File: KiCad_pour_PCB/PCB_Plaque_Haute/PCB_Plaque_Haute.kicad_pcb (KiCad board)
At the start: 2 copper layers, 108 x 108 mm, 9 parts

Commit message: Avancement carte PCB
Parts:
- moved Servomoteur1 24.0 mm to (192.5, 100.0)
- moved Servomoteur2 23.5 mm to (196.5, 100.0)
- moved Arduino_Nano1 20.5 mm to (170.8, 91.4)
- moved Bloc_pile1 20.5 mm to (180.5, 73.5)
- moved Inter_Input1 20.5 mm to (179.5, 84.0)
- moved Inter_in_c1 20.5 mm to (182.5, 80.0)
- moved BMP1 17.7 mm to (131.3, 114.2)
- moved MPU1 16.4 mm to (131.4, 97.0)
- moved Inter_plaques1 12.6 mm to (116.0, 86.3)
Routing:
- net Net-(BMP1-GND): track 259.1 -> 250.5 mm
- net Net-(Arduino_Nano1-Vin): track 167.1 -> 174.8 mm
- net Net-(BMP1-VCC): track 45.9 -> 40.4 mm
- net Net-(BMP1-SDA): track 34.6 -> 29.7 mm
- net Net-(BMP1-SCL): track 37.6 -> 33.8 mm
- net Net-(Arduino_Nano1-D10): track 43.0 -> 39.5 mm
- net Net-(Arduino_Nano1-5V): track 13.9 -> 10.9 mm
- net Net-(Arduino_Nano1-D9): track 53.7 -> 52.4 mm
- net Net-(Arduino_Nano1-D4): track 37.4 -> 36.6 mm
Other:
- board size 108 x 108 mm -> 94 x 94 mm
- board text added: "A4 A5 Vin GND 5V"
- board text added: "GND AN 5V"
- board text added: "GND D2 D3 D4 D6 D7"
- board text added: "SW2 SW1 Jack"

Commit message: PCB_Fin
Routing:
- net Net-(BMP1-GND): track 250.5 -> 251.1 mm
- added copper zone on B.Cu, net Net-(BMP1-GND)
- added copper zone on F.Cu, net Net-(BMP1-GND)
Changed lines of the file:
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@@
 			(outputformat 1)
 			(mirror no)
-			(drillshape 1)
+			(drillshape 0)
 			(scaleselection 1)
-			(outputdirectory "")
+			(outputdirectory "Fab/")
 		)
 	)
@@
 			(layer "F.SilkS")
 		)
+		(fp_rect
+			(start -1.4 -14.6)
+			(end 19 1.2)
+			(stroke
+				(width 0.1)
+				(type default)
+			)
+			(fill none)
+			(layer "F.SilkS")
+		)
 		(fp_line
 			(start 19.05 1.27)
@@
 		)
 		(fp_text user "${REFERENCE}"
+			(at 3.73 9.77 180)
+			(unlocked yes)
+			(layer "F.Fab")
+			(effects
+				(font
+					(size 1 1)
+					(thickness 0.15)
+				)
+			)
+		)
+		(fp_text user "${REFERENCE}"
 			(at 3.89 -7.01 90)
 			(unlocked yes)
@@
 			(at 10.16 0 180)
 			(size 1.524 1.524)
-			(drill 0.762)
+			(drill 1)
 			(layers "*.Cu" "*.Mask")
 			(remove_unused_layers no)
@@
 			(at 12.7 0 180)
 			(size 1.524 1.524)
-			(drill 0.762)
+			(drill 1)
 			(layers "*.Cu" "*.Mask")
 			(remove_unused_layers no)
@@
 			(at 15.24 0 180)
 			(size 1.524 1.524)
-			(drill 0.762)
+			(drill 1)
 			(layers "*.Cu" "*.Mask")
 			(remove_unused_layers no)
@@
 			(at 17.78 0 180)
 			(size 1.524 1.524)
-			(drill 0.762)
+			(drill 1)
 			(layers "*.Cu" "*.Mask")
 			(remove_unused_layers no)
@@
 			(layer "F.SilkS")
 		)
+		(fp_rect
+			(start -1.2 -14.6)
+			(end 8.8 1.2)
+			(stroke
+				(width 0.1)
+				(type default)
+			)
+			(fill none)
+			(layer "F.SilkS")
+		)
 		(fp_line
 			(start 8.89 1.27)
@@
 			)
 		)
-		(pad "" np_thru_hole circle
-			(at -2.54 -15.24 270)
-			(size 2.3 2.3)
-			(drill 1.78)
-			(layers "F&B.Cu" "*.Mask")
-		)
-		(pad "" np_thru_hole circle
-			(at -2.54 0 270)
-			(size 2.3 2.3)
-			(drill 1.78)
-			(layers "F&B.Cu" "*.Mask")
-		)
-		(pad "" np_thru_hole circle
-			(at 38.1 -15.24 270)
-			(size 2.3 2.3)
-			(drill 1.78)
-			(layers "F&B.Cu" "*.Mask")
-		)
-		(pad "" np_thru_hole circle
-			(at 38.1 0 270)
-			(size 2.3 2.3)
-			(drill 1.78)
-			(layers "F&B.Cu" "*.Mask")
-		)
 		(pad "1" thru_hole rect
 			(at 0 0)
@@
 	)
 	(segment
-		(start 179.5 82)
-		(end 179.5 84)
+		(start 199 98)
+		(end 199 101)
 		(width 0.2)
 		(layer "F.Cu")
@@
 	)
 	(segment
-		(start 199 98)
-		(end 199 101)
+		(start 192.98 93.98)
+		(end 194.98 93.98)
 		(width 0.2)
 		(layer "F.Cu")
@@
 	)
 	(segment
-		(start 192.98 93.98)
-		(end 194.98 93.98)
+		(start 180.5 72.5)
+		(end 179.5 72.5)
 		(width 0.2)
 		(layer "F.Cu")
@@
 	)
 	(segment
-		(start 178.5 81)
-		(end 179.5 82)
-		(width 0.2)
-		(layer "F.Cu")
-		(net 19)
-	)
-	(segment
 		(start 111.19 90.14)
 		(end 111.19 104.52)
@@
 	)
 	(segment
-		(start 180.5 72.5)
-		(end 178.5 74.5)
+		(start 194.98 93.98)
+		(end 199 98)
 		(width 0.2)
 		(layer "F.Cu")
@@
 	)
 	(segment
-		(start 194.98 93.98)
-		(end 199 98)
+		(start 116 87.33)
+		(end 123.5 87.33)
 		(width 0.2)
 		(layer "F.Cu")
@@
 	)
 	(segment
-		(start 116 87.33)
-		(end 123.5 87.33)
+		(start 178.5 81)
+		(end 179.5 82)
 		(width 0.2)
 		(layer "F.Cu")
@@
 	)
 	(segment
+		(start 178.5 73.5)
+		(end 178.5 81)
+		(width 0.2)
+		(layer "F.Cu")
+		(net 19)
+	)
+	(segment
 		(start 189.49 81.924314)
 		(end 189.49 90.49)
@@
 	)
 	(segment
+		(start 179.5 82)
+		(end 179.5 84)
+		(width 0.2)
+		(layer "F.Cu")
+		(net 19)
+	)
+	(segment
 		(start 187.08 132)
 		(end 189 130.08)
@@
 	)
 	(segment
-		(start 178.5 74.5)
-		(end 178.5 81)
+		(start 179.5 72.5)
+		(end 178.5 73.5)
 		(width 0.2)
 		(layer "F.Cu")
@@
 		(net 33)
 	)
+	(zone
+		(net 19)
+		(net_name "Net-(BMP1-GND)")
+		(layers "F&B.Cu")
+		(name "Plan_Masse")
+		(hatch none 0.5)
+		(connect_pads
+			(clearance 0.5)
+		)
+		(min_thickness 0.25)
+		(filled_areas_thickness no)
+		(fill yes
+			(thermal_gap 0.5)
+			(thermal_bridge_width 0.5)
+		)
+		(polygon
+			(pts
+				(xy 99 154) (xy 226 154) (xy 227 153) (xy 227 39.5) (xy 103 39.5) (xy 99 43.5)
+			)
+		)
+	)
 )

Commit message: Nouvelle version PCB _ Suite RCE3
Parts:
- removed BMP1: ~, INSARIANNE_Lib:BMP180
- removed Inter_in_c1: ~, Connector_PinHeader_1.00mm:PinHeader_1x03_P1.00mm_Vertical
- removed Inter_plaques1: ~, Connector_PinHeader_1.00mm:PinHeader_1x05_P1.00mm_Vertical
- removed MPU1: ~, INSARIANNE_Lib:MPU6050
- added Inter_Cap_Vol1: ~, Connector_PinHeader_2.54mm:PinHeader_1x02_P2.54mm_Vertical, F.Cu at (185.0, 79.2)
- added Octocoupleur1: ~, INSARIANNE_Lib:Octocoupleur, F.Cu at (170.0, 75.8)
- Bloc_pile1: footprint Connector_PinHeader_1.00mm:PinHeader_1x02_P1.00mm_Vertical -> Connector_PinHeader_2.54mm:PinHeader_1x02_P2.54mm_Vertical
- Inter_Input1: footprint Connector_PinHeader_1.00mm:PinHeader_1x06_P1.00mm_Vertical -> Connector_PinHeader_2.54mm:PinHeader_1x06_P2.54mm_Vertical
- Servomoteur1, Servomoteur2: footprint Connector_PinHeader_1.00mm:PinHeader_1x03_P1.00mm_Vertical -> Connector_PinHeader_2.54mm:PinHeader_1x03_P2.54mm_Vertical
- moved Inter_Input1 15.9 mm to (195.0, 87.7), turned to 0 degrees
- moved Bloc_pile1 13.0 mm to (190.7, 81.5), turned to 90 degrees
- moved Servomoteur1 7.53 mm to (191.5, 107.5)
- moved Servomoteur2 7.53 mm to (197.5, 107.5)
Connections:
- Arduino_Nano1 pad 11: unconnected-(Arduino_Nano1-D8-Pad11) -> Net-(Arduino_Nano1-D8)
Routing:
- net Net-(Arduino_Nano1-Vin): track 174.8 -> 11.9 mm
- net Net-(Bloc_pile1-GND): track 251.1 -> 92.9 mm
- net Net-(Arduino_Nano1-D8): track 0.00 -> 43.6 mm
- net Net-(BMP1-VCC): track 40.4 -> 0.00 mm
- net Net-(BMP1-SCL): track 33.8 -> 0.00 mm
- net Net-(BMP1-SDA): track 29.7 -> 0.00 mm
- net Net-(Arduino_Nano1-D6): track 36.2 -> 53.1 mm
- net Net-(Arduino_Nano1-D7): track 38.3 -> 55.0 mm
- net Net-(Arduino_Nano1-D4): track 36.6 -> 48.9 mm
- net Net-(Arduino_Nano1-D3): track 32.7 -> 43.7 mm
- net Net-(Arduino_Nano1-D2): track 29.2 -> 39.3 mm
- net Net-(Arduino_Nano1-D10): track 39.5 -> 30.7 mm
- net Net-(Inter_Cap_Vol1-GND): track 0.00 -> 8.42 mm
- net Net-(Inter_Cap_Vol1-Cap): track 0.00 -> 8.42 mm
- net Net-(Arduino_Nano1-5V): track 10.9 -> 17.9 mm
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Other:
- board text removed: "A4 A5 Vin GND 5V"
- board text removed: "SW2 SW1 Jack"

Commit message: Fin carte PCB
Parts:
- moved Octocoupleur1 2.84 mm to (170.0, 73.0)
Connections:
- Inter_Cap_Vol1 pad 1: Net-(Inter_Cap_Vol1-GND) -> Net-(Inter_Cap_Vol1-5V)
- Octocoupleur1 pad 3: Net-(Inter_Cap_Vol1-Cap) -> unconnected-(Octocoupleur1-NC-Pad3)
- Octocoupleur1 pad 4: Net-(Inter_Cap_Vol1-GND) -> unconnected-(Octocoupleur1-Base-Pad4)
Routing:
- net Net-(Inter_Cap_Vol1-5V): track 0.00 -> 8.54 mm
- net Net-(Inter_Cap_Vol1-GND): track 8.42 -> 0.00 mm
- net Net-(Bloc_pile1-GND): track 92.9 -> 96.1 mm
- net Net-(Arduino_Nano1-D8): track 43.6 -> 46.5 mm
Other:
- board text added: "2023/2024"
- board text added: "INS'aéro"
- board text added: "PCB_Plaque_Haute INSARIANNE1"

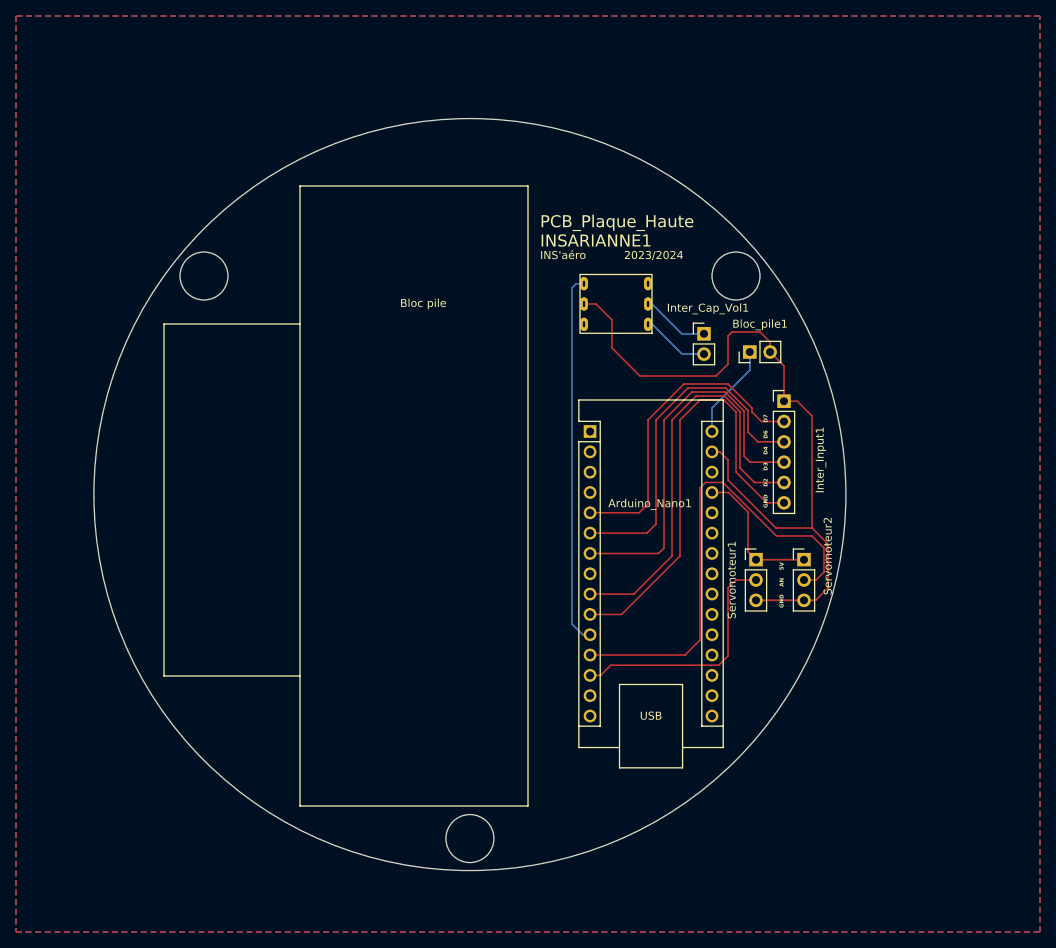
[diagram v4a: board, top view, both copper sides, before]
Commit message: Correction trous de perçage PCB Truc stupide d'un triangle équilatérales Plus besoin de faire des trous manuellement
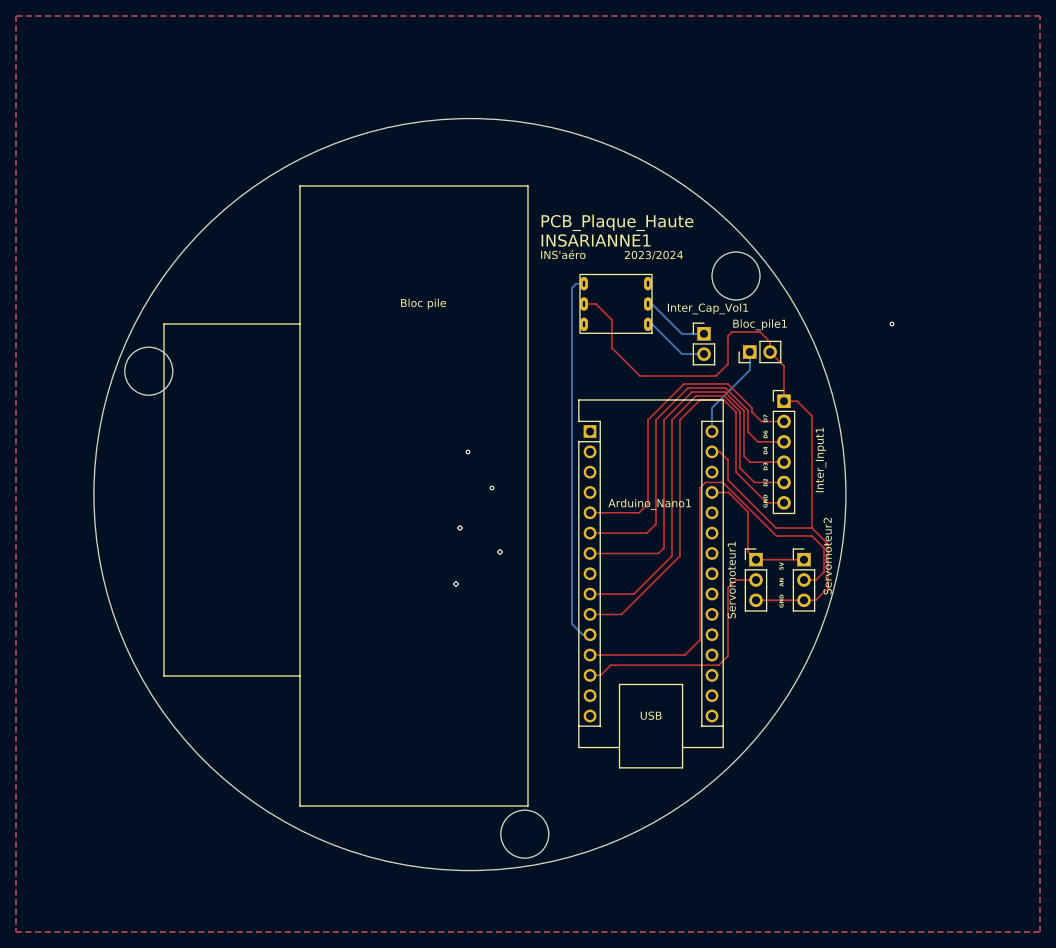
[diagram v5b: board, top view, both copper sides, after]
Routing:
- net Net-(Bloc_pile1-GND): vias 0 -> 11
- net (no net): vias 0 -> 1
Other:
- outline, holes or cut-outs redrawn
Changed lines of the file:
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@@
 	)
 	(gr_circle
-		(center 122.5 72)
-		(end 125.5 72)
+		(center 115.6 83.9)
+		(end 118.6 83.9)
 		(stroke
 			(width 0.1)
@@
 	)
 	(gr_circle
-		(center 155.74 142.32)
-		(end 158.74 142.32)
+		(center 162.6 141.77)
+		(end 165.6 141.77)
 		(stroke
 			(width 0.1)
@@
 		(fill none)
 		(layer "User.2")
+	)
+	(gr_line
+		(start 189 72)
+		(end 162.61 141.77)
+		(stroke
+			(width 0.1)
+			(type default)
+		)
+		(layer "User.3")
+	)
+	(gr_circle
+		(center 155.74 99.32)
+		(end 177.24 99.32)
+		(stroke
+			(width 0.1)
+			(type default)
+		)
+		(fill none)
+		(layer "User.3")
+	)
+	(gr_line
+		(start 115.6 83.92)
+		(end 189 72)
+		(stroke
+			(width 0.1)
+			(type default)
+		)
+		(layer "User.3")
+	)
+	(gr_line
+		(start 162.61 141.77)
+		(end 115.6 83.92)
+		(stroke
+			(width 0.1)
+			(type default)
+		)
+		(layer "User.3")
 	)
 	(gr_text "PCB_Plaque_Haute\nINSARIANNE1"
@@
 		)
 	)
+	(via
+		(at 208.5 78)
+		(size 0.6)
+		(drill 0.3)
+		(layers "F.Cu" "B.Cu")
+		(net 0)
+	)
 	(segment
 		(start 195 92.73)
@@
 		(net 5)
 	)
+	(via
+		(at 159.5 106.5)
+		(size 0.6)
+		(drill 0.3)
+		(layers "F.Cu" "B.Cu")
+		(free yes)
+		(net 5)
+	)
+	(via
+		(at 154 110.5)
+		(size 0.6)
+		(drill 0.3)
+		(layers "F.Cu" "B.Cu")
+		(free yes)
+		(net 5)
+	)
+	(via
+		(at 154.5 103.5)
+		(size 0.6)
+		(drill 0.3)
+		(layers "F.Cu" "B.Cu")
+		(free yes)
+		(net 5)
+	)
+	(via
+		(at 154 110.5)
+		(size 0.6)
+		(drill 0.3)
+		(layers "F.Cu" "B.Cu")
+		(free yes)
+		(net 5)
+	)
+	(via
+		(at 154 110.5)
+		(size 0.6)
+		(drill 0.3)
+		(layers "F.Cu" "B.Cu")
+		(free yes)
+		(net 5)
+	)
+	(via
+		(at 154.5 103.5)
+		(size 0.6)
+		(drill 0.3)
+		(layers "F.Cu" "B.Cu")
+		(free yes)
+		(net 5)
+	)
+	(via
+		(at 159.5 106.5)
+		(size 0.6)
+		(drill 0.3)
+		(layers "F.Cu" "B.Cu")
+		(free yes)
+		(net 5)
+	)
+	(via
+		(at 158.5 98.5)
+		(size 0.6)
+		(drill 0.3)
+		(layers "F.Cu" "B.Cu")
+		(free yes)
+		(net 5)
+	)
+	(via
+		(at 159.5 106.5)
+		(size 0.6)
+		(drill 0.3)
+		(layers "F.Cu" "B.Cu")
+		(free yes)
+		(net 5)
+	)
+	(via
+		(at 155.5 94)
+		(size 0.6)
+		(drill 0.3)
+		(layers "F.Cu" "B.Cu")
+		(free yes)
+		(net 5)
+	)
+	(via
+		(at 154 110.5)
+		(size 0.6)
+		(drill 0.3)
+		(layers "F.Cu" "B.Cu")
+		(free yes)
+		(net 5)
+	)
